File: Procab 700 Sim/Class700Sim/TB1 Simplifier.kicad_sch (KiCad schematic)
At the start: 0 parts

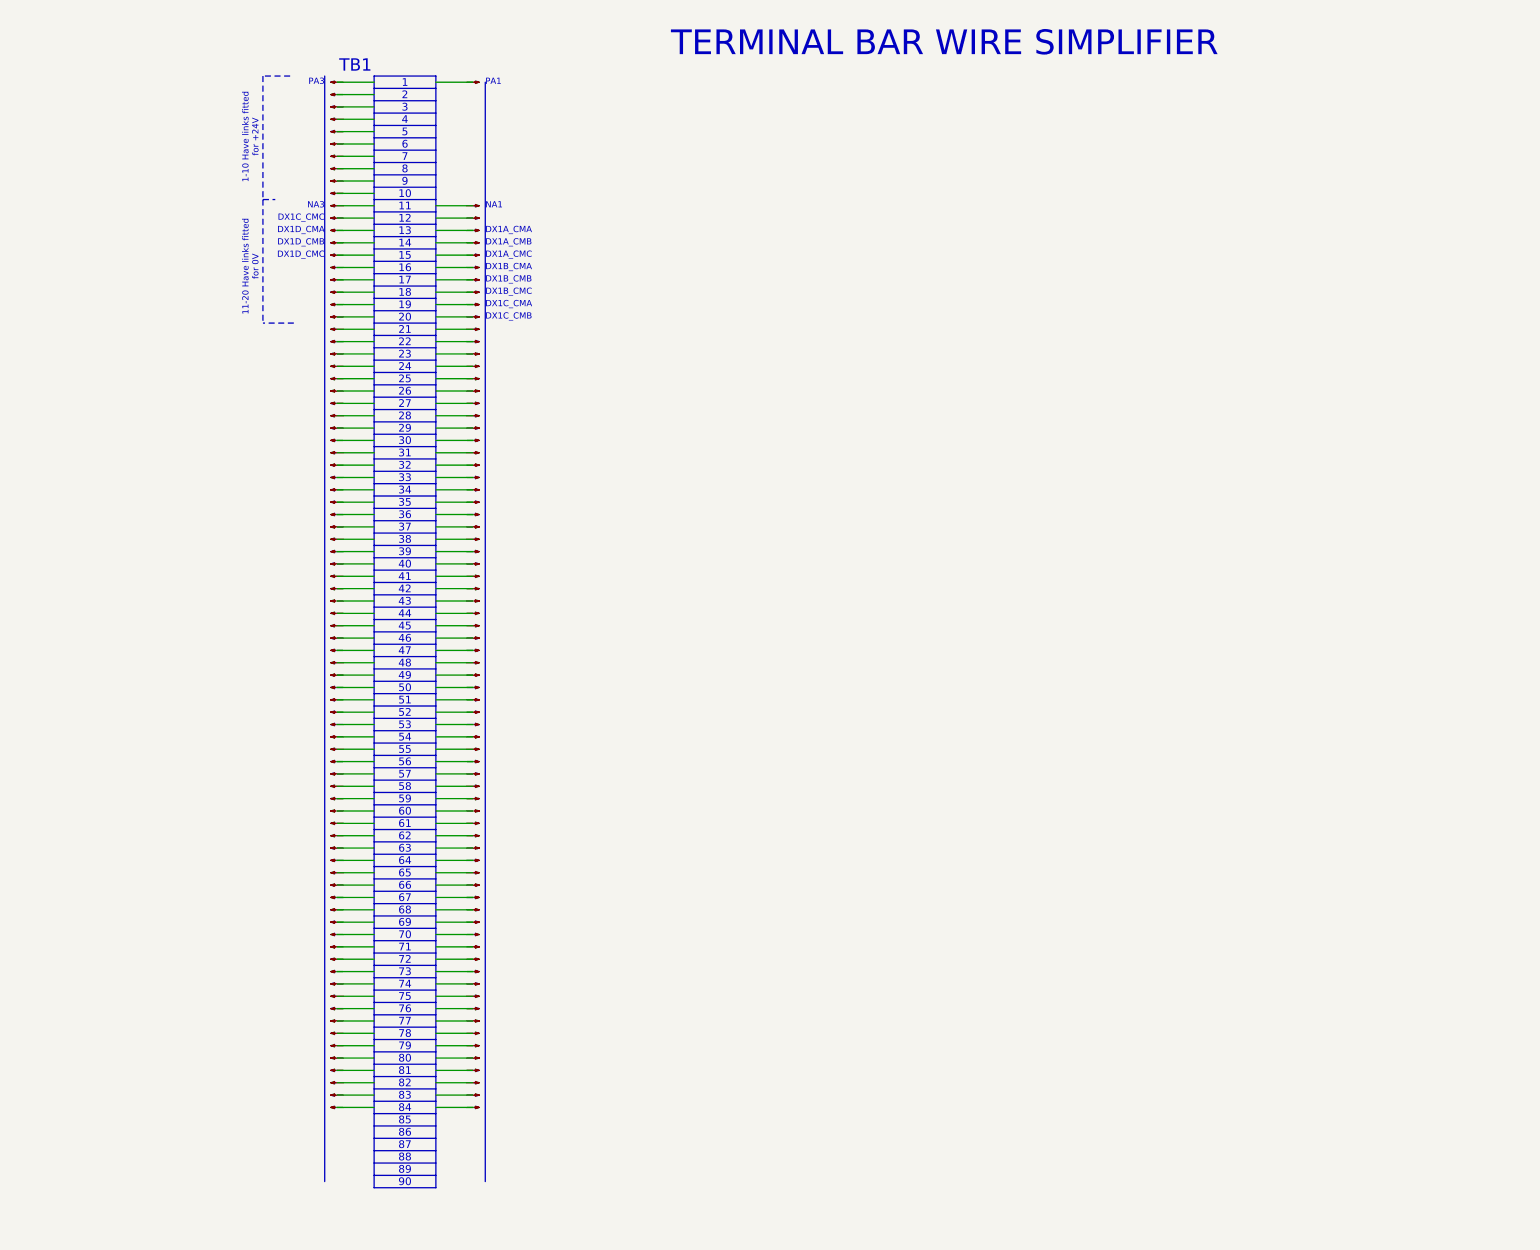
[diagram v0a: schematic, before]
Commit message: Drew Main Driving Panel
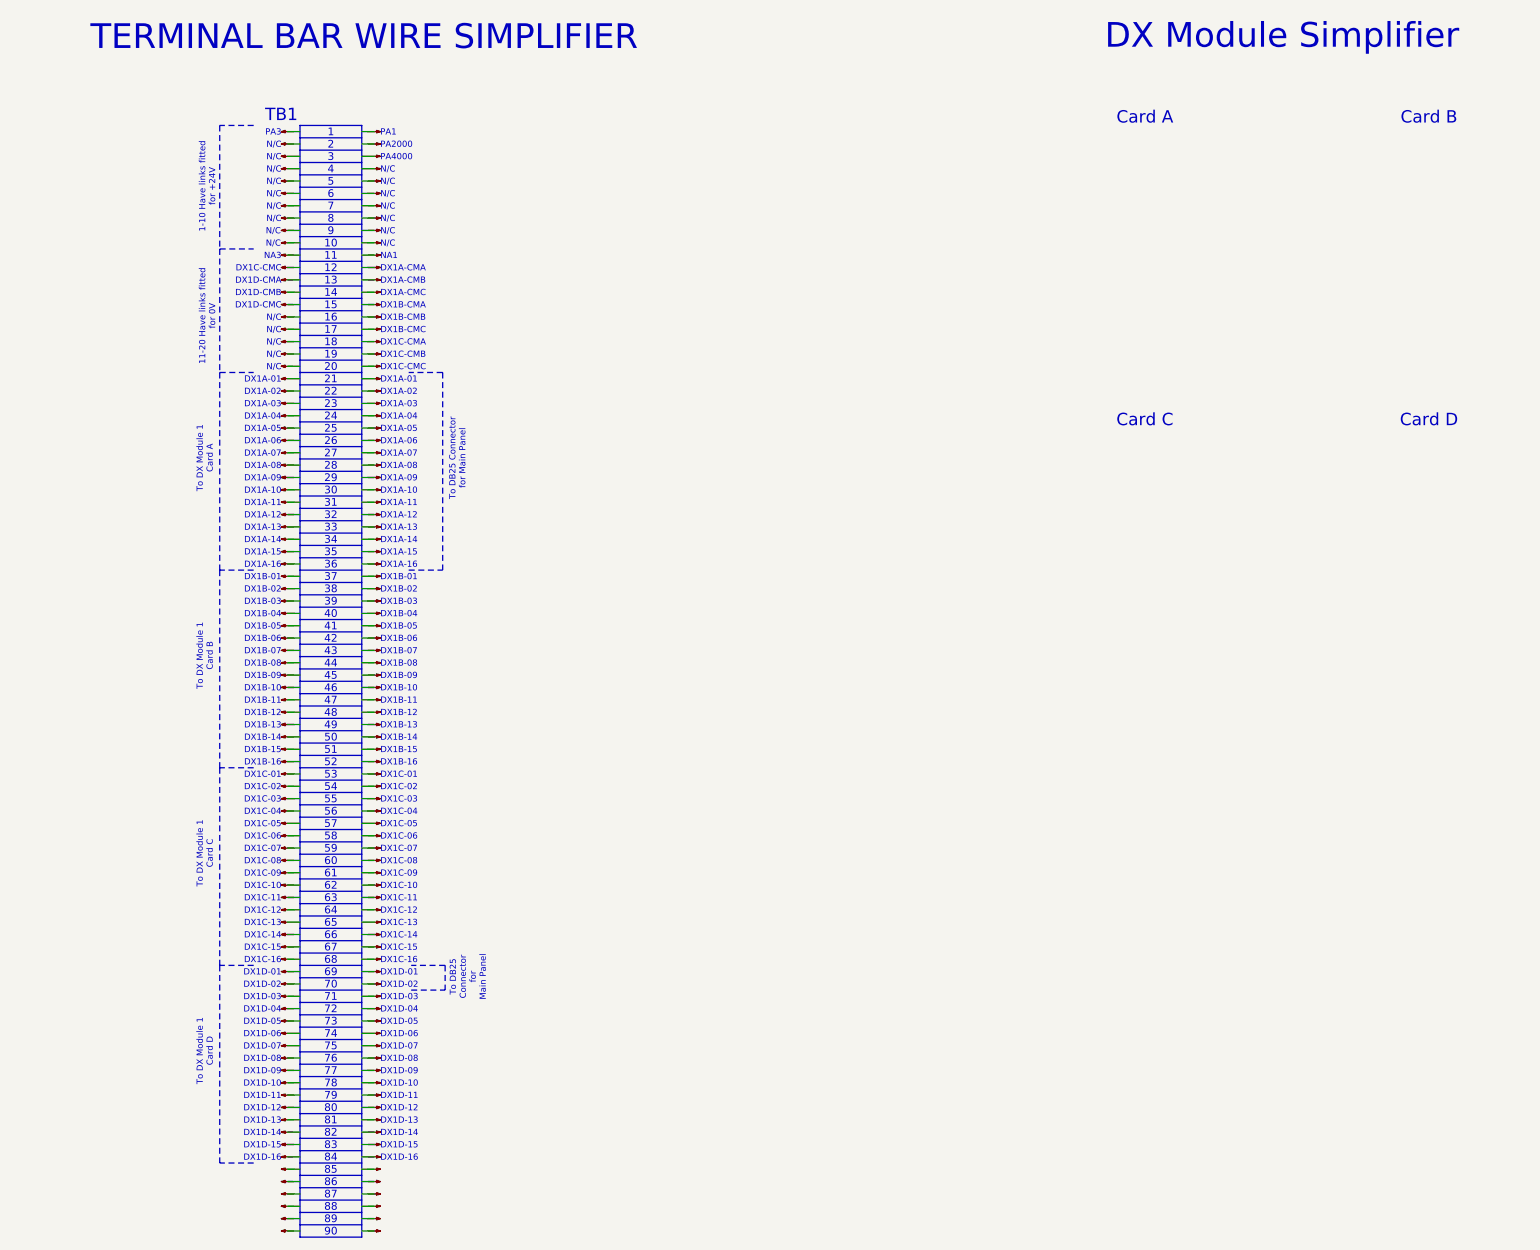
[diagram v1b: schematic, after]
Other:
- note added: "Card A"
- note added: "Card B"
- note added: "Card C"
- note added: "Card D"
- note added: "DX Module Simplifier"
- note added: "DX1A-01"
- note added: "DX1A-02"
- note added: "DX1A-03"
- note added: "DX1A-04"
- note added: "DX1A-05"
- note added: "DX1A-06"
- note added: "DX1A-07"
- note added: "DX1A-08"
- note added: "DX1A-09"
- note added: "DX1A-10"
- note added: "DX1A-11"
- note added: "DX1A-12"
- note added: "DX1A-13"
- note added: "DX1A-14"
- note added: "DX1A-15"
- note added: "DX1A-16"
- note added: "DX1A-CMA"
- note added: "DX1A-CMB"
- note added: "DX1A-CMC"
- note added: "DX1B-01"
- note added: "DX1B-02"
- note added: "DX1B-03"
- note added: "DX1B-04"
- note added: "DX1B-05"
- note added: "DX1B-06"
- note added: "DX1B-07"
- note added: "DX1B-08"
- note added: "DX1B-09"
- note added: "DX1B-10"
- note added: "DX1B-11"
- note added: "DX1B-12"
- note added: "DX1B-13"
- note added: "DX1B-14"
- note added: "DX1B-15"
- note added: "DX1B-16"
- note added: "DX1B-CMA"
- note added: "DX1B-CMB"
- note added: "DX1B-CMC"
- note added: "DX1C-01"
- note added: "DX1C-02"
- note added: "DX1C-03"
- note added: "DX1C-04"
- note added: "DX1C-05"
- note added: "DX1C-06"
- note added: "DX1C-07"
- note added: "DX1C-08"
- note added: "DX1C-09"
- note added: "DX1C-10"
- note added: "DX1C-11"
- note added: "DX1C-12"
- note added: "DX1C-13"
- note added: "DX1C-14"
- note added: "DX1C-15"
- note added: "DX1C-16"
- note added: "DX1C-CMA"
- note added: "DX1C-CMB"
- note added: "DX1C-CMC"
- note added: "DX1D-01"
- note added: "DX1D-02"
- note added: "DX1D-03"
- note added: "DX1D-04"
- note added: "DX1D-05"
- note added: "DX1D-06"
- note added: "DX1D-07"
- note added: "DX1D-08"
- note added: "DX1D-09"
- note added: "DX1D-10"
- note added: "DX1D-11"
- note added: "DX1D-12"
- note added: "DX1D-13"
- note added: "DX1D-14"
- note added: "DX1D-15"
- note added: "DX1D-16"
- note added: "DX1D-CMA"
- note added: "DX1D-CMB"
- note added: "DX1D-CMC"
- note added: "N/C"
- note added: "PA2000"
- note added: "PA4000"
- note added: "To DB25 Connector for Main Panel"
- note added: "To DX Module 1 Card A"
- note added: "To DX Module 1 Card B"
- note added: "To DX Module 1 Card C"
- note added: "To DX Module 1 Card D"
- note removed: "DX1A_CMA"
- note removed: "DX1A_CMB"
- note removed: "DX1A_CMC"
- note removed: "DX1B_CMA"
- note removed: "DX1B_CMB"
- note removed: "DX1B_CMC"
- note removed: "DX1C_CMA"
- note removed: "DX1C_CMB"
- note removed: "DX1C_CMC"
- note removed: "DX1D_CMA"
- note removed: "DX1D_CMB"
- note removed: "DX1D_CMC"
- title: (none) -> Class 700 Compact Simulator Electrical

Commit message: Changes made
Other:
- note added: "PA5000"
- note added: "PA6000"
- note added: "To Air Gauge Panel"

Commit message: TB2 added
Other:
- note added: "40 39 38 37 36 35 34 33 32 31 30 29 28 27 26 25 24 23 22 21 20 19 18 17 16 15 14 13 12 11 10 9 8 7 6 5 4 3 2 1"
- note added: "90 89 88 87 86 85 84 83 82 81 80 79 78 77 76 75 74 73 72 71 70 69 68 67 66 65 64 63 62 61 60 59 58 57 56 55 54 53 52 51 50 49 48 47 46 45 44 43 42 41"
- note removed: "1 2 3 4 5 6 7 8 9 10 11 12 13 14 15 16 17 18 19 20 21 22 23 24 25 26 27 28 29 30 31 32 33 34 35 36 37 38 39 40"
- note removed: "41 42 43 44 45 46 47 48 49 50 51 52 53 54 55 56 57 58 59 60 61 62 63 64 65 66 67 68 69 70 71 72 73 74 75 76 77 78 79 80 81 82 83 84 85 86 87 88 89 90"
